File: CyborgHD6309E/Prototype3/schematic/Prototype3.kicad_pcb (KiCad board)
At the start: 2 copper layers, 95 x 72 mm, 33 parts, among them J1 Conn_I2C_Master, J2 Conn_Micro_SD, J3 Conn_USB_Serial, J4 Conn_AVR_ISP, J5 Conn_AVR_ISP, SW1 USR_SW, U1 ATmega1284P-PU, U2 HM628128DLP-5, U3 HD63C09E, U4 ATmega328P-PU, Y1 20MHz, Y2 20MHz

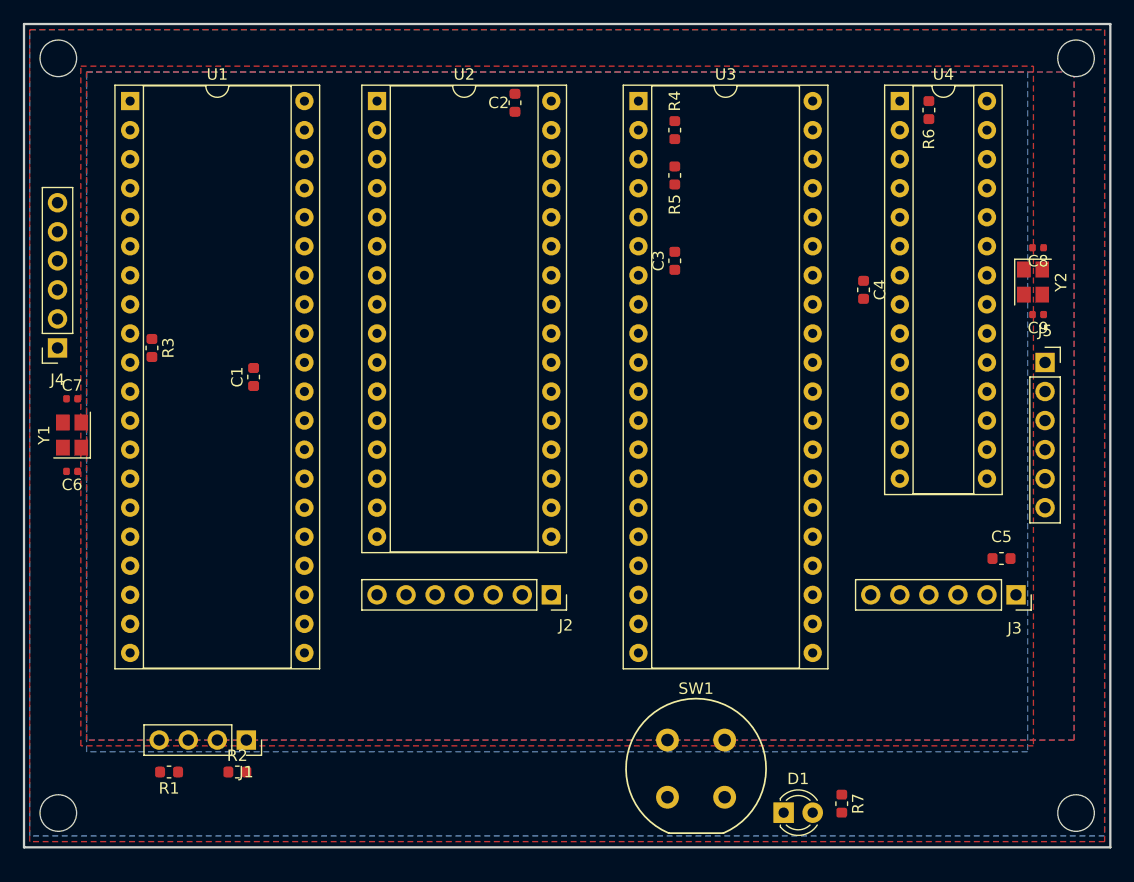
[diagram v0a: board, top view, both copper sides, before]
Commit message: [CyborgHD6309E] Update Prototype3 pins
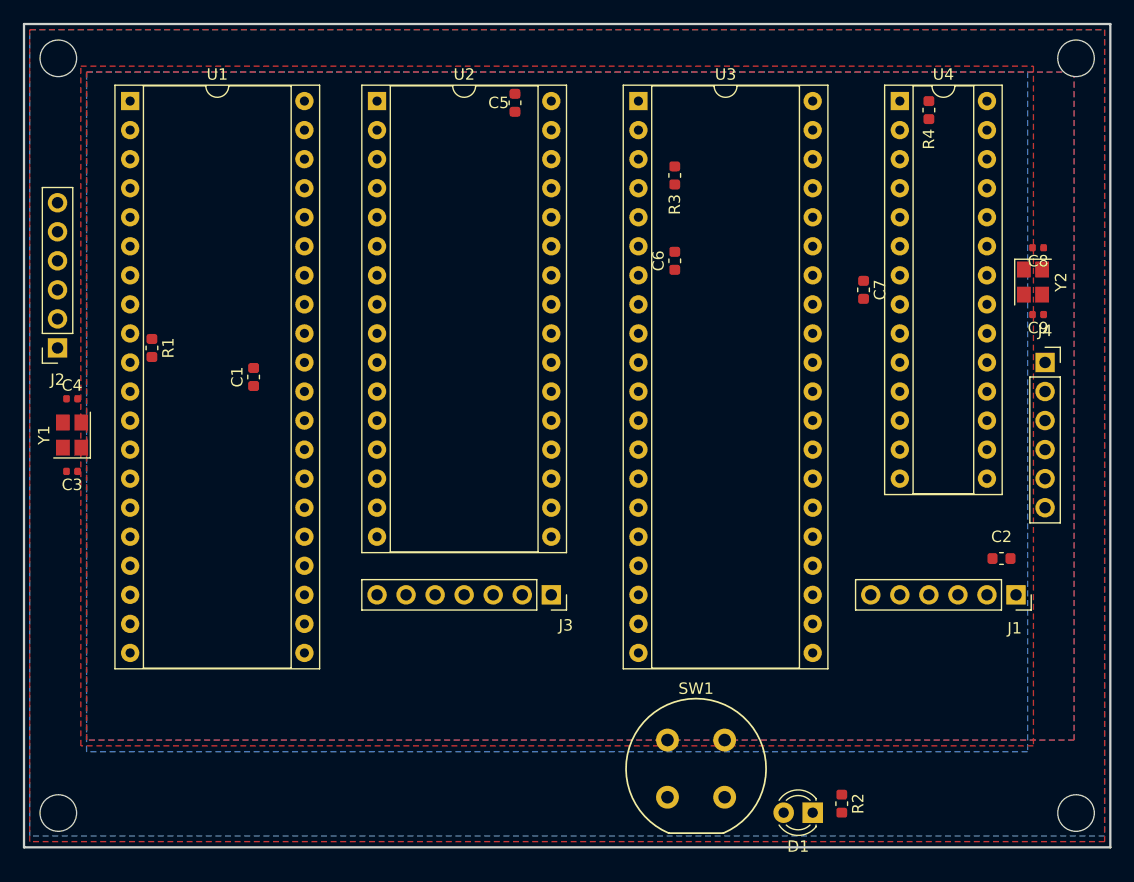
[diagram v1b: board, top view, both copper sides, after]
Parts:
- removed the J1 at (120.4, 132.6)
- removed the R1 at (113.7, 135.4)
- removed the R2 at (119.7, 135.4)
- removed the R4 at (157.9, 79.3)
- moved D1 2.54 mm to (170.0, 139.0), turned to 180 degrees
- renumbered C5 to C2, C6 to C3, C7 to C4, C2 to C5, C3 to C6, C4 to C7, J3 to J1, J4 to J2, J2 to J3, J5 to J4, R3 to R1, R7 to R2, R5 to R3, R6 to R4
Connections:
- net /~ACK renamed /~ACK~
- net /~INT renamed /~INT~
- net /~SD_CS renamed /~SD_CS~
- net /~STEP renamed /~STEP~
- D1 pad 1: /~USR_LED~ -> Net-(D1-Pad1)
- D1 pad 2: Net-(D1-Pad2) -> /USR_LED
- J4 pad 1: Net-(J5-Pad1) -> Net-(J4-Pad1)
- R2 pad 1: VCC -> GND
- R2 pad 2: Net-(D1-Pad2) -> Net-(D1-Pad1)
- R4 pad 1: VCC -> Net-(J4-Pad1)
- R4 pad 2: Net-(J5-Pad1) -> VCC
- U1 pad 1: /~HALT -> /~NMI~
- U1 pad 18: /~USR_LED~ -> /USR_LED
- U1 pad 19: /LIC -> /~RAM_E~
- U1 pad 22: /SCL -> /~RESET~
- U1 pad 23: /SDA -> /~HALT~
- U1 pad 24: /A1 -> /RD_WR
- U1 pad 25: /A0 -> /BUSY
- U1 pad 28: /~RAM_E -> /LIC
- U1 pad 3: /~RESET -> /A0
- U1 pad 32: Net-(U1-Pad32) -> (no net)
- U1 pad 4: /RD_WR -> /A1
- U2 pad 10: /A10 -> /A2
- U2 pad 11: /A11 -> /A1
- U2 pad 12: /A12 -> /A0
- U2 pad 13: /D5 -> /D0
- U2 pad 14: /D6 -> /D1
- U2 pad 15: /D7 -> /D2
- U2 pad 17: /D4 -> /D3
- U2 pad 18: /D3 -> /D4
- U2 pad 19: /D2 -> /D5
- U2 pad 20: /D1 -> /D6
- U2 pad 21: /D0 -> /D7
- U2 pad 22: /~RAM_E -> /~RAM_E~
- U2 pad 23: /A2 -> /A10
- U2 pad 25: /A1 -> /A11
- U2 pad 26: /A0 -> /A9
- U2 pad 27: /A15 -> /A8
- U2 pad 28: /A14 -> /A13
- U2 pad 3: /A3 -> /A14
- U2 pad 31: /A13 -> /A15
- U2 pad 4: /A4 -> /A12
- U2 pad 5: /A5 -> /A7
- U2 pad 7: /A7 -> /A5
- U2 pad 8: /A8 -> /A4
- U2 pad 9: /A9 -> /A3
- U3 pad 2: Net-(R4-Pad1) -> /~NMI~
- U3 pad 33: (no net) -> /BUSY
- U3 pad 37: /~RESET -> /~RESET~
- U3 pad 40: /~HALT -> /~HALT~
- U4 pad 1: Net-(J5-Pad1) -> Net-(J4-Pad1)
- U4 pad 21: Net-(U4-Pad21) -> (no net)
- U4 pad 23: Net-(U4-Pad23) -> (no net)
